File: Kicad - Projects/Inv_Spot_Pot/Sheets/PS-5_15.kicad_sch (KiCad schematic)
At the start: 23 parts, among them U2 LTV-817S

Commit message: Adicionado Footprint do Transformador
Footprint do transformador adicionada

Linha dos capacitores XY adicionada

Alteração nas linhas de PWM
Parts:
- removed T3: (no value), Transformer_THT:Custom_Transformer-10P-EEL22_EE30_7, symbol Custom_Transformers:Transformer_1P_2S_CT
- added C23: 100n, Capacitor_SMD:C_1206_3216Metric_Pad1.33x1.80mm_HandSolder, symbol Device:C
- added C6: 220u, Capacitor_THT:CP_Radial_D8.0mm_P3.50mm, symbol Device:C_Polarized
- added D18: SS16, Diode_SMD:D_SOD-128, symbol Device:D_Schottky
- added R23: 10k, Resistor_SMD:R_1206_3216Metric_Pad1.30x1.75mm_HandSolder, symbol Device:R
- added T3: (no value), Transformer_THT:Transformer_Breve_TEZ-28x33, symbol Custom_Transformers:Transformer_1P_3S_CT
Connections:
- net 310V: now also T3.1
- net GND: now also CY3.2; no longer CY3.1
- net ~{GND}: now also CY3.1, T3.7, T3.9; no longer CY3.2
- net at C14.2, D2.2 (A), U1.5 (drain)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: now also T3.2
- net at D4.2 (A): now also T3.6
- net at D6.2 (A): now also T3.8
- new net: D18.2 (A), T3.5
- new net 24V: C23.2, C6.1, D18.1 (K), R23.2
- new net GND_{24V}: C23.1, C6.2, R23.1, T3.4
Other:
- moved on the sheet: C10, C11, C12, C13, C14, C5, C7, C8, C9, CY3, D2, D4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

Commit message: Adicionado LM7805 7V->5V
Adicionado na placa de display um regulador linear de 5V para a alimentação do display

Rota atual:
7V -> 5V -> 3V (53,9mA max medido, cálculo p/ 61mA)
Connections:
- net 5V renamed 7V
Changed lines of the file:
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@@
 		)
 	)
-	(hierarchical_label "5V"
+	(hierarchical_label "7V"
 		(shape input)
 		(at 187.96 69.85 0)

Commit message: Updates
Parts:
- F2: footprint Connector_PinHeader_2.54mm:PinHeader_1x02_P2.54mm_Vertical -> Connector_JST:JST_XA_B02B-XASK-1-A_1x02_P2.50mm_Vertical
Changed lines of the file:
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@@
 			)
 		)
-		(property "Footprint" "Connector_PinHeader_2.54mm:PinHeader_1x02_P2.54mm_Vertical"
+		(property "Footprint" "Connector_JST:JST_XA_B02B-XASK-1-A_1x02_P2.50mm_Vertical"
 			(at 199.39 91.44 0)
 			(hide yes)

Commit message: Cotações
Cotações
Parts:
- C13: value 47p -> 4.7n
- D4: footprint Diode_SMD:D_SOD-128 -> Diode_SMD:D_SMB
- F2: footprint Connector_JST:JST_XA_B02B-XASK-1-A_1x02_P2.50mm_Vertical -> Connector_PinHeader_2.54mm:PinHeader_1x02_P2.54mm_Vertical
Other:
- moved on the sheet: D18
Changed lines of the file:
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@@
 	)
 	(junction
-		(at 107.95 91.44)
-		(diameter 0)
-		(color 0 0 0 0)
-	)
-	(junction
 		(at 82.55 68.58)
 		(diameter 0)
@@
 	)
 	(junction
+		(at 107.95 91.44)
+		(diameter 0)
+		(color 0 0 0 0)
+	)
+	(junction
 		(at 157.48 90.17)
 		(diameter 0)
@@
 	(wire
 		(pts
-			(xy 115.57 91.44) (xy 107.95 91.44)
+			(xy 111.76 91.44) (xy 107.95 91.44)
 		)
 		(stroke
@@
 	(wire
 		(pts
+			(xy 119.38 91.44) (xy 123.19 91.44)
+		)
+		(stroke
+			(width 0)
+			(type default)
+		)
+	)
+	(wire
+		(pts
 			(xy 80.01 46.99) (xy 109.22 46.99)
 		)
@@
 			)
 		)
-		(property "Value" "47p"
+		(property "Value" "4.7n"
 			(at 99.06 58.4201 0)
 			(show_name no)
@@
 			)
 		)
-		(property "Footprint" "Diode_SMD:D_SOD-128"
+		(property "Footprint" "Diode_SMD:D_SMB"
 			(at 149.86 69.85 0)
 			(hide yes)
@@
 			)
 		)
-		(property "Footprint" "Connector_JST:JST_XA_B02B-XASK-1-A_1x02_P2.50mm_Vertical"
+		(property "Footprint" "Connector_PinHeader_2.54mm:PinHeader_1x02_P2.54mm_Vertical"
 			(at 199.39 91.44 0)
 			(hide yes)
@@
 	(symbol
 		(lib_id "Device:D_Schottky")
-		(at 119.38 91.44 0)
+		(at 115.57 91.44 0)
 		(mirror x)
 		(unit 1)
@@
 		(dnp no)
 		(property "Reference" "D18"
-			(at 119.0625 97.79 0)
+			(at 115.2525 97.79 0)
 			(show_name no)
 			(do_not_autoplace no)
@@
 		)
 		(property "Value" "SS16"
-			(at 119.0625 95.25 0)
+			(at 115.2525 95.25 0)
 			(show_name no)
 			(do_not_autoplace no)
@@
 		)
 		(property "Footprint" "Diode_SMD:D_SOD-128"
-			(at 119.38 91.44 0)
+			(at 115.57 91.44 0)
 			(hide yes)
 			(show_name no)
@@
 		)
 		(property "Datasheet" ""
-			(at 119.38 91.44 0)
+			(at 115.57 91.44 0)
 			(hide yes)
 			(show_name no)
@@
 		)
 		(property "Description" "Schottky diode"
-			(at 119.38 91.44 0)
+			(at 115.57 91.44 0)
 			(hide yes)
 			(show_name no)

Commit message: Atualização de Footprint
Atualizados footrpints do capacitor da fonte auxiliar e do transformador toroidal
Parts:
- C10: value 47u -> 100u; footprint Capacitor_THT:CP_Radial_D8.0mm_P3.50mm -> Capacitor_THT:CP_Radial_D18.0mm_P7.50mm
- F2: footprint Connector_PinHeader_2.54mm:PinHeader_1x02_P2.54mm_Vertical -> Connector_JST:JST_XH_B2B-XH-A_1x02_P2.50mm_Vertical
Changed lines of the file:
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@@
 		)
 		(instances
-			(project "Inv_Spot_Pot"
+			(project "Inv_Spot_Pot - A"
 				(path "/e27abe51-96c0-4fdf-ba00-b5a281cd0e9c/d2713cc2-b69d-489c-ab73-ea3982f94a63"
 					(reference "C6")
@@
 		)
 		(instances
-			(project "Inv_Spot_Pot"
+			(project "Inv_Spot_Pot - A"
 				(path "/e27abe51-96c0-4fdf-ba00-b5a281cd0e9c/d2713cc2-b69d-489c-ab73-ea3982f94a63"
 					(reference "C13")
@@
 		)
 		(instances
-			(project "Inv_Spot_Pot"
+			(project "Inv_Spot_Pot - A"
 				(path "/e27abe51-96c0-4fdf-ba00-b5a281cd0e9c/d2713cc2-b69d-489c-ab73-ea3982f94a63"
 					(reference "C11")
@@
 		)
 		(instances
-			(project "Inv_Spot_Pot"
+			(project "Inv_Spot_Pot - A"
 				(path "/e27abe51-96c0-4fdf-ba00-b5a281cd0e9c/d2713cc2-b69d-489c-ab73-ea3982f94a63"
 					(reference "R23")
@@
 		)
 		(instances
-			(project "Inv_Spot_Pot"
+			(project "Inv_Spot_Pot - A"
 				(path "/e27abe51-96c0-4fdf-ba00-b5a281cd0e9c/d2713cc2-b69d-489c-ab73-ea3982f94a63"
 					(reference "R14")
@@
 		)
 		(instances
-			(project "Inv_Spot_Pot"
+			(project "Inv_Spot_Pot - A"
 				(path "/e27abe51-96c0-4fdf-ba00-b5a281cd0e9c/d2713cc2-b69d-489c-ab73-ea3982f94a63"
 					(reference "C14")
@@
 		)
 		(instances
-			(project "Inv_Spot_Pot"
+			(project "Inv_Spot_Pot - A"
 				(path "/e27abe51-96c0-4fdf-ba00-b5a281cd0e9c/d2713cc2-b69d-489c-ab73-ea3982f94a63"
 					(reference "D4")
@@
 		)
 		(instances
-			(project "Inv_Spot_Pot"
+			(project "Inv_Spot_Pot - A"
 				(path "/e27abe51-96c0-4fdf-ba00-b5a281cd0e9c/d2713cc2-b69d-489c-ab73-ea3982f94a63"
 					(reference "R12")
@@
 		)
 		(instances
-			(project "Inv_Spot_Pot"
+			(project "Inv_Spot_Pot - A"
 				(path "/e27abe51-96c0-4fdf-ba00-b5a281cd0e9c/d2713cc2-b69d-489c-ab73-ea3982f94a63"
 					(reference "C12")
@@
 		)
 		(instances
-			(project "Inv_Spot_Pot"
+			(project "Inv_Spot_Pot - A"
 				(path "/e27abe51-96c0-4fdf-ba00-b5a281cd0e9c/d2713cc2-b69d-489c-ab73-ea3982f94a63"
 					(reference "U1")
@@
 		)
 		(instances
-			(project "Inv_Spot_Pot"
+			(project "Inv_Spot_Pot - A"
 				(path "/e27abe51-96c0-4fdf-ba00-b5a281cd0e9c/d2713cc2-b69d-489c-ab73-ea3982f94a63"
 					(reference "D9")
@@
 			)
 		)
-		(property "Footprint" "Connector_PinHeader_2.54mm:PinHeader_1x02_P2.54mm_Vertical"
+		(property "Footprint" "Connector_JST:JST_XH_B2B-XH-A_1x02_P2.50mm_Vertical"
 			(at 199.39 91.44 0)
 			(hide yes)
@@
 		)
 		(instances
-			(project "Inv_Spot_Pot"
+			(project "Inv_Spot_Pot - A"
 				(path "/e27abe51-96c0-4fdf-ba00-b5a281cd0e9c/d2713cc2-b69d-489c-ab73-ea3982f94a63"
 					(reference "F2")
@@
 		)
 		(instances
-			(project "Inv_Spot_Pot"
+			(project "Inv_Spot_Pot - A"
 				(path "/e27abe51-96c0-4fdf-ba00-b5a281cd0e9c/d2713cc2-b69d-489c-ab73-ea3982f94a63"
 					(reference "D2")
@@
 		)
 		(instances
-			(project "Inv_Spot_Pot"
+			(project "Inv_Spot_Pot - A"
 				(path "/e27abe51-96c0-4fdf-ba00-b5a281cd0e9c/d2713cc2-b69d-489c-ab73-ea3982f94a63"
 					(reference "C9")
@@
 		)
 		(instances
-			(project "Inv_Spot_Pot"
+			(project "Inv_Spot_Pot - A"
 				(path "/e27abe51-96c0-4fdf-ba00-b5a281cd0e9c/d2713cc2-b69d-489c-ab73-ea3982f94a63"
 					(reference "CY3")
@@
 		)
 		(instances
-			(project "Inv_Spot_Pot"
+			(project "Inv_Spot_Pot - A"
 				(path "/e27abe51-96c0-4fdf-ba00-b5a281cd0e9c/d2713cc2-b69d-489c-ab73-ea3982f94a63"
 					(reference "C8")
@@
 		)
 		(instances
-			(project "Inv_Spot_Pot"
+			(project "Inv_Spot_Pot - A"
 				(path "/e27abe51-96c0-4fdf-ba00-b5a281cd0e9c/d2713cc2-b69d-489c-ab73-ea3982f94a63"
 					(reference "T3")
@@
 		)
 		(instances
-			(project "Inv_Spot_Pot"
+			(project "Inv_Spot_Pot - A"
 				(path "/e27abe51-96c0-4fdf-ba00-b5a281cd0e9c/d2713cc2-b69d-489c-ab73-ea3982f94a63"
 					(reference "R8")
@@
 		)
 		(instances
-			(project "Inv_Spot_Pot"
+			(project "Inv_Spot_Pot - A"
 				(path "/e27abe51-96c0-4fdf-ba00-b5a281cd0e9c/d2713cc2-b69d-489c-ab73-ea3982f94a63"
 					(reference "U2")
@@
 			)
 		)
-		(property "Value" "47u"
+		(property "Value" "100u"
 			(at 87.63 57.15 0)
 			(show_name no)
@@
 			)
 		)
-		(property "Footprint" "Capacitor_THT:CP_Radial_D8.0mm_P3.50mm"
+		(property "Footprint" "Capacitor_THT:CP_Radial_D18.0mm_P7.50mm"
 			(at 81.28 53.6448 0)
 			(hide yes)
@@
 		)
 		(instances
-			(project "Inv_Spot_Pot"
+			(project "Inv_Spot_Pot - A"
 				(path "/e27abe51-96c0-4fdf-ba00-b5a281cd0e9c/d2713cc2-b69d-489c-ab73-ea3982f94a63"
 					(reference "C10")
@@
 		)
 		(instances
-			(project "Inv_Spot_Pot"
+			(project "Inv_Spot_Pot - A"
 				(path "/e27abe51-96c0-4fdf-ba00-b5a281cd0e9c/d2713cc2-b69d-489c-ab73-ea3982f94a63"
 					(reference "C5")
@@
 		)
 		(instances
-			(project "Inv_Spot_Pot"
+			(project "Inv_Spot_Pot - A"
 				(path "/e27abe51-96c0-4fdf-ba00-b5a281cd0e9c/d2713cc2-b69d-489c-ab73-ea3982f94a63"
 					(reference "D18")
@@
 		)
 		(instances
-			(project "Inv_Spot_Pot"
+			(project "Inv_Spot_Pot - A"
 				(path "/e27abe51-96c0-4fdf-ba00-b5a281cd0e9c/d2713cc2-b69d-489c-ab73-ea3982f94a63"
 					(reference "C23")
@@
 		)
 		(instances
-			(project "Inv_Spot_Pot"
+			(project "Inv_Spot_Pot - A"
 				(path "/e27abe51-96c0-4fdf-ba00-b5a281cd0e9c/d2713cc2-b69d-489c-ab73-ea3982f94a63"
 					(reference "C7")
@@
 		)
 		(instances
-			(project "Inv_Spot_Pot"
+			(project "Inv_Spot_Pot - A"
 				(path "/e27abe51-96c0-4fdf-ba00-b5a281cd0e9c/d2713cc2-b69d-489c-ab73-ea3982f94a63"
 					(reference "R15")
@@
 		)
 		(instances
-			(project "Inv_Spot_Pot"
+			(project "Inv_Spot_Pot - A"
 				(path "/e27abe51-96c0-4fdf-ba00-b5a281cd0e9c/d2713cc2-b69d-489c-ab73-ea3982f94a63"
 					(reference "D6")
@@
 		)
 		(instances
-			(project "Inv_Spot_Pot"
+			(project "Inv_Spot_Pot - A"
 				(path "/e27abe51-96c0-4fdf-ba00-b5a281cd0e9c/d2713cc2-b69d-489c-ab73-ea3982f94a63"
 					(reference "R7")

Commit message: Exploração da Placa de Potência
Explorando diferentes posições para os componentes da placa de potência
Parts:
- removed C14: 100n, Capacitor_SMD:C_1206_3216Metric_Pad1.33x1.80mm_HandSolder, symbol Device:C
- removed D18, D6: SS16, Diode_SMD:D_SOD-128, symbol Device:D_Schottky
- removed D2: K7, Diode_SMD:D_SMA_Handsoldering, symbol Device:D_Schottky
- removed D4: SS16, Diode_SMD:D_SMB, symbol Device:D_Schottky
- added D2, D3, D4, D5: US1M, Diode_SMD:D_SMA, symbol Diode:US1M
- renumbered D9 to D6
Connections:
- net 24V: now also D4.1 (K)
- net 310V: now also D5.2 (A)
- net 7V: now also D2.1 (K)
- net at C13.1, R12.2: now also D5.1 (K)
- net at T3.6: now also D2.2 (A)
- net at C7.1, F2.1, R15.1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: now also D3.1 (K)
- net at T3.5: now also D4.2 (A)
- net at T3.8: now also D3.2 (A)
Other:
- moved on the sheet: C10, CY3

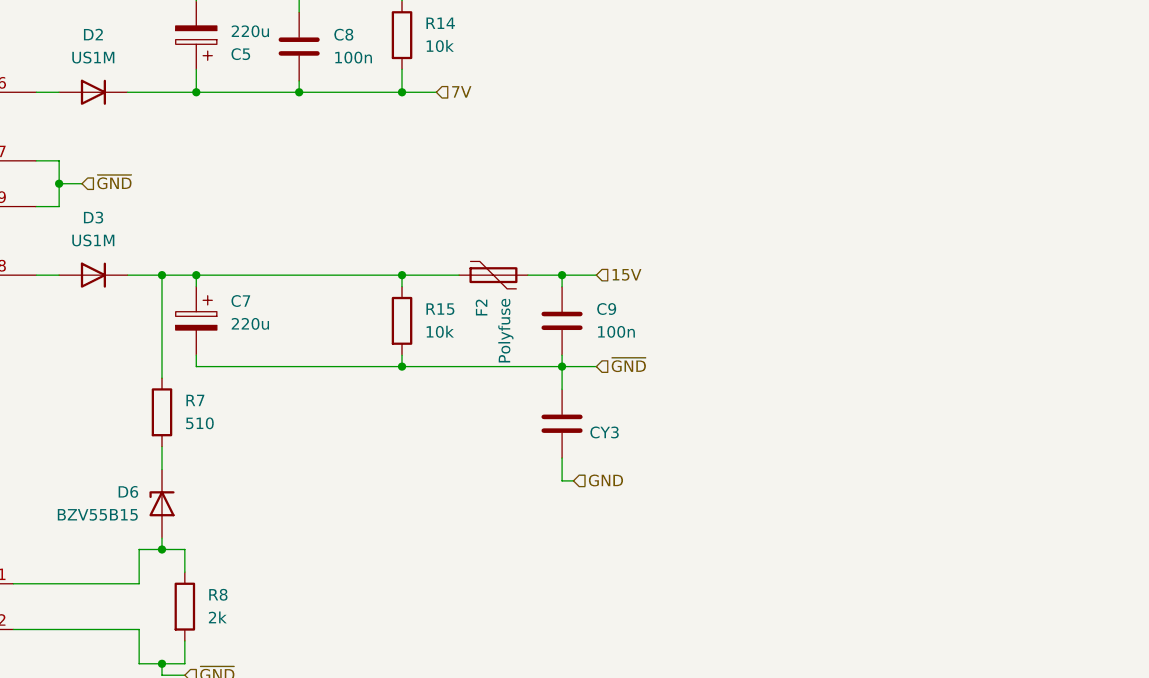
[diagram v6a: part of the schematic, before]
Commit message: Adicionada Fuaração
Adicionada furação de montagem na placa de display, 4 furos M3 nos cantos da placa
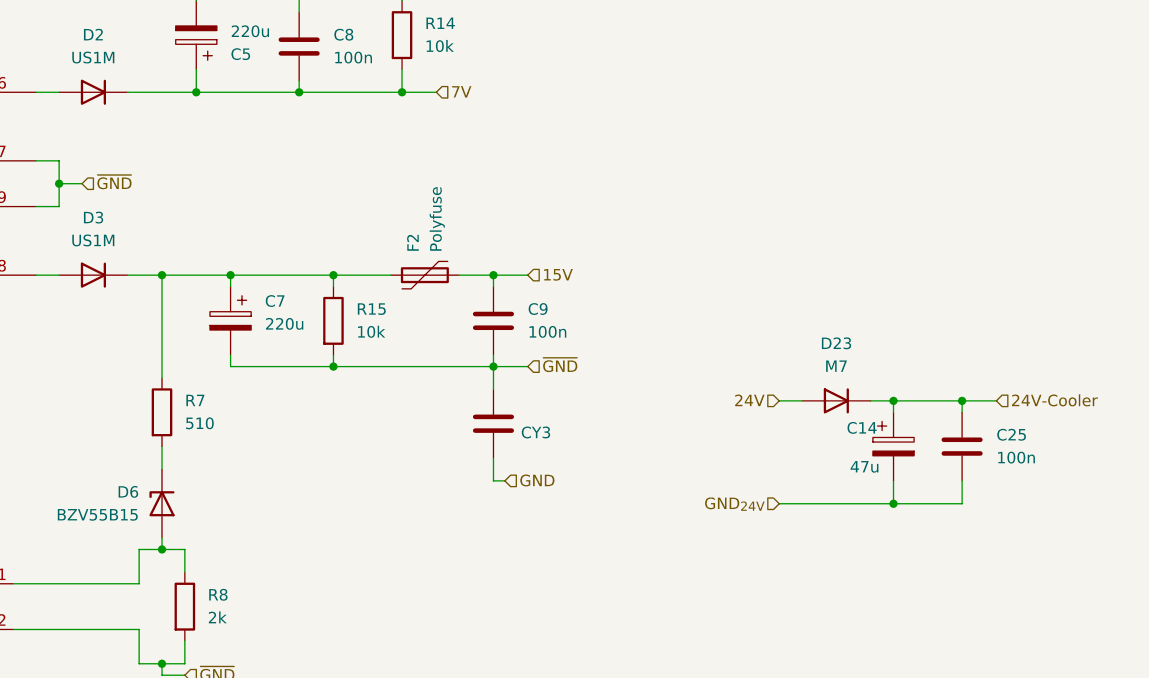
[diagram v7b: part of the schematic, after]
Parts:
- added C14: 47u, Capacitor_THT:CP_Radial_D6.3mm_P2.50mm, symbol Device:C_Polarized
- added C25: 100n, Capacitor_SMD:C_1206_3216Metric_Pad1.33x1.80mm_HandSolder, symbol Device:C
- added D23: M7, Diode_SMD:D_SMA, symbol Device:D
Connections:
- net 24V: now also D23.2 (A)
- net GND_{24V}: now also C14.2, C25.2
- new net 24V-Cooler: C14.1, C25.1, D23.1 (K)
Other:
- moved on the sheet: C7, C9, CY3, F2, R15

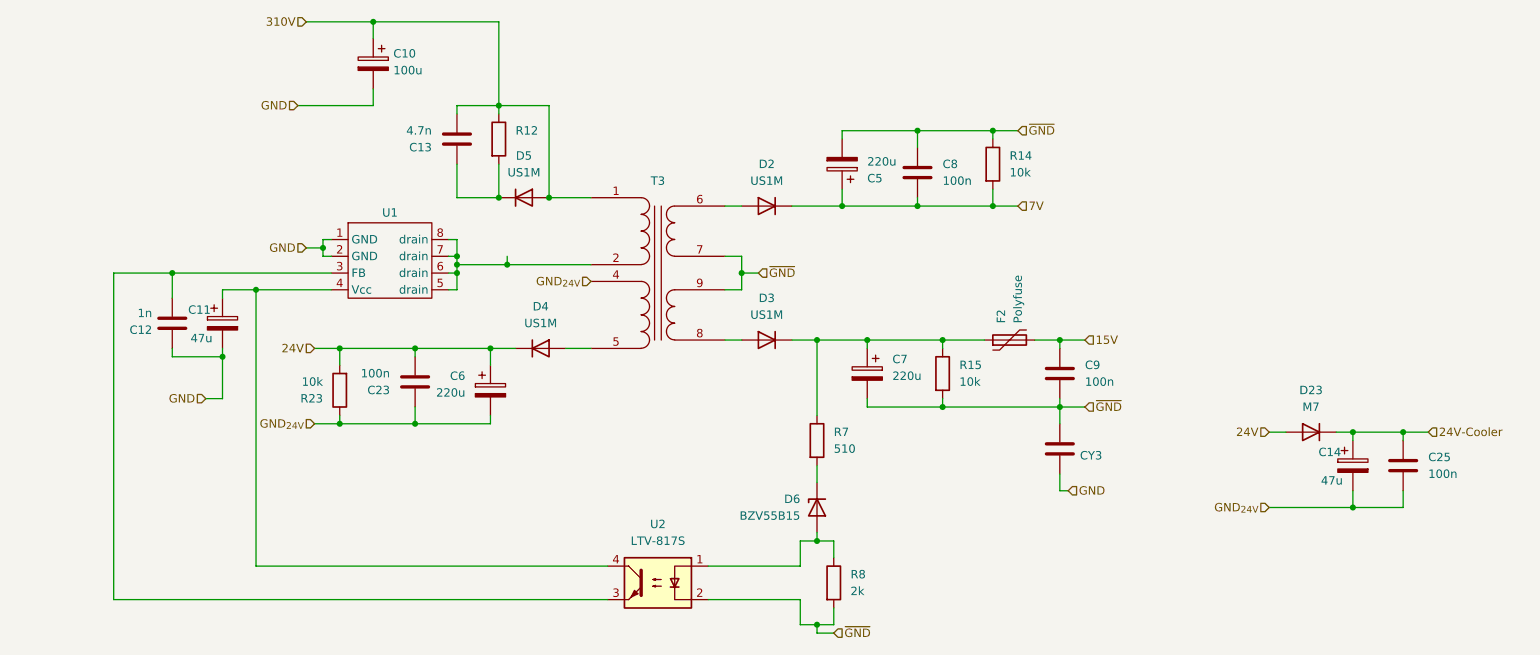
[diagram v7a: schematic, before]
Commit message: Finalização da Nova Placa de Potência
Dissipadores reorientados e reposicionados para melhor fluxo de ar

Ajuste dos footprints para dissipadores

Adição de resistores na placa de display para melhor proteção do STM32 e redução do brilho da LCD
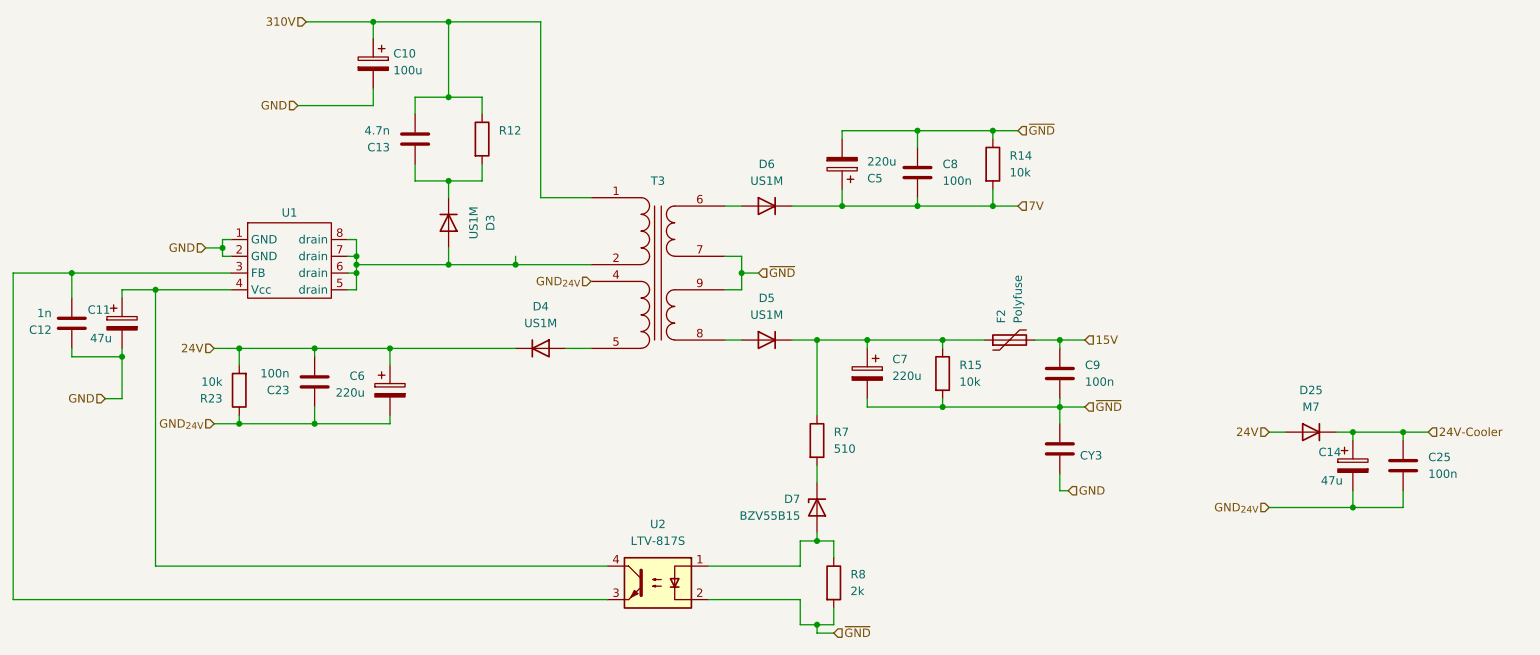
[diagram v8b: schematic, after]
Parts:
- F2: footprint Connector_JST:JST_XH_B2B-XH-A_1x02_P2.50mm_Vertical -> Connector_PinHeader_2.54mm:PinHeader_1x02_P2.54mm_Vertical
- renumbered D23 to D25, D5 to D3, D3 to D5, D2 to D6, D6 to D7
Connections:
- net 310V: no longer D3.2 (A)
- net at T3.2, U1.5 (drain), U1.6 (drain)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: now also D3.2 (A)
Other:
- moved on the sheet: C11, C12, C13, C23, C6, D3, R12, R23, U1
